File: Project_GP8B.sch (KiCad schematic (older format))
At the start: 16 parts, among them U1 74AHC05, U2 74AHC05, U3 74AHC1G02, U5 74AHC05

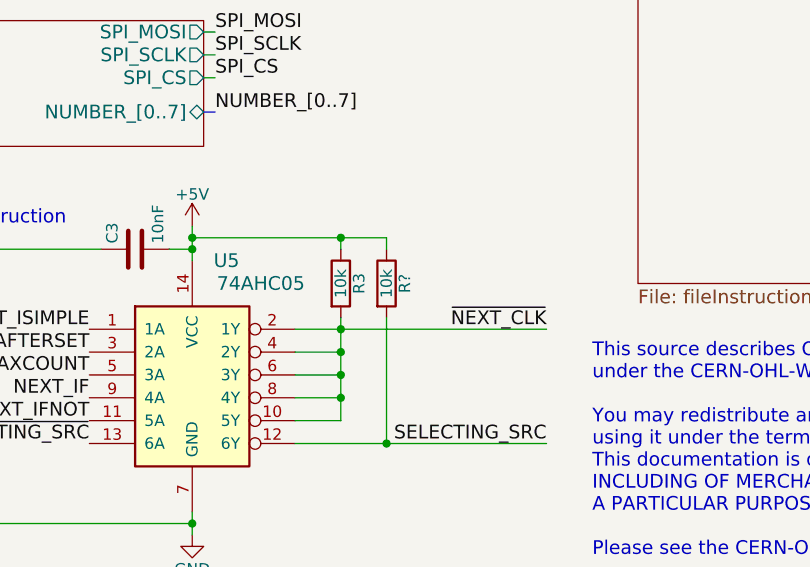
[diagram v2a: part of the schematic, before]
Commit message: Remove weird ghost bus in register
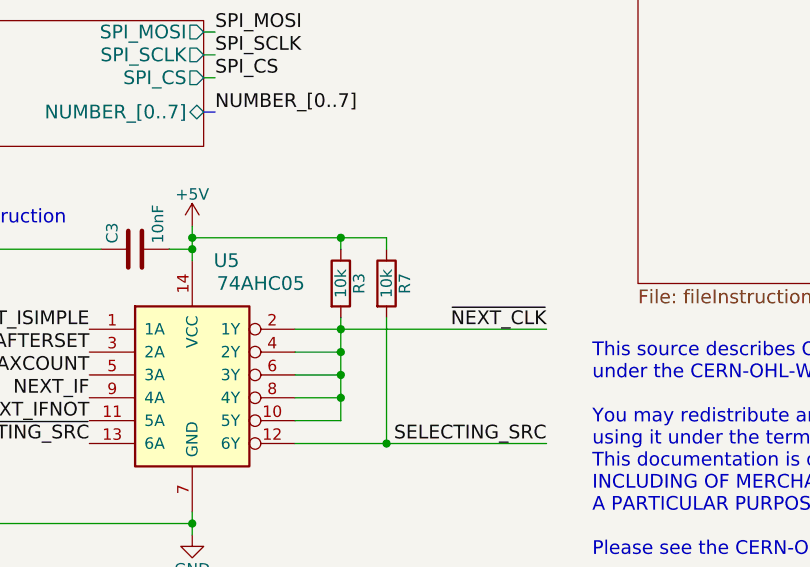
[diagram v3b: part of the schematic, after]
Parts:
- gave numbers to parts that had none: 1
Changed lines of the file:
@@
 SELECTING_SRC
 $Comp
-L Device:R R?
+L Device:R R7
 U 1 1 60507EBE
 P 6600 5250
-F 0 "R?" V 6680 5250 50  0000 C CNN
+F 0 "R7" V 6680 5250 50  0000 C CNN
 F 1 "10k" V 6600 5250 50  0000 C CNN
 F 2 "Resistor_SMD:R_0805_2012Metric" V 6530 5250 50  0001 C CNN

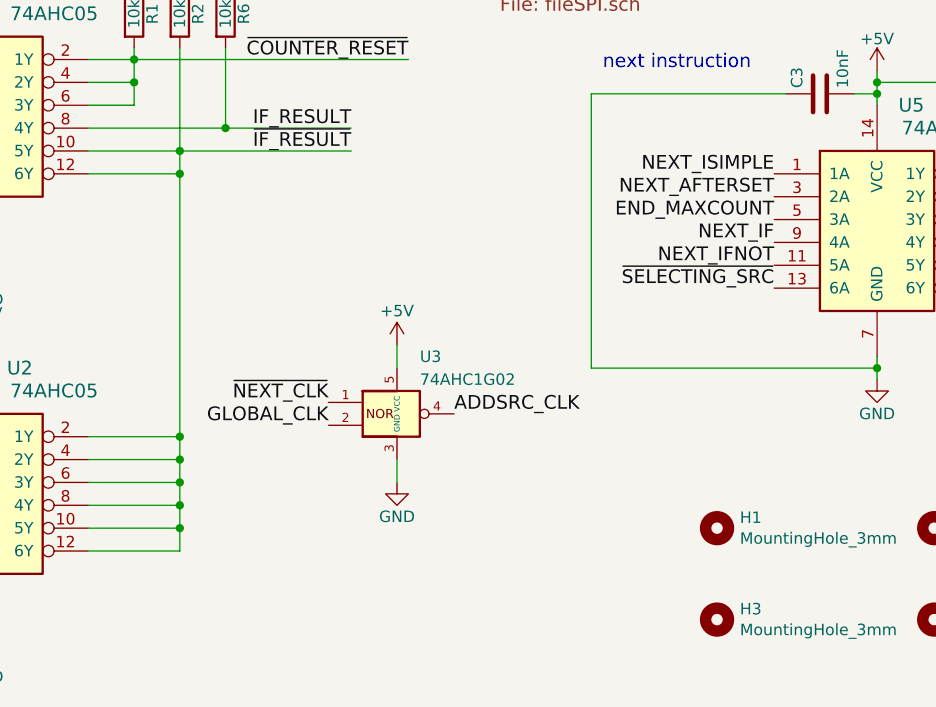
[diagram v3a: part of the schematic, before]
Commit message: Go next only if SRCVALUE, (complex instruction) #8 adding 74AHC1G08
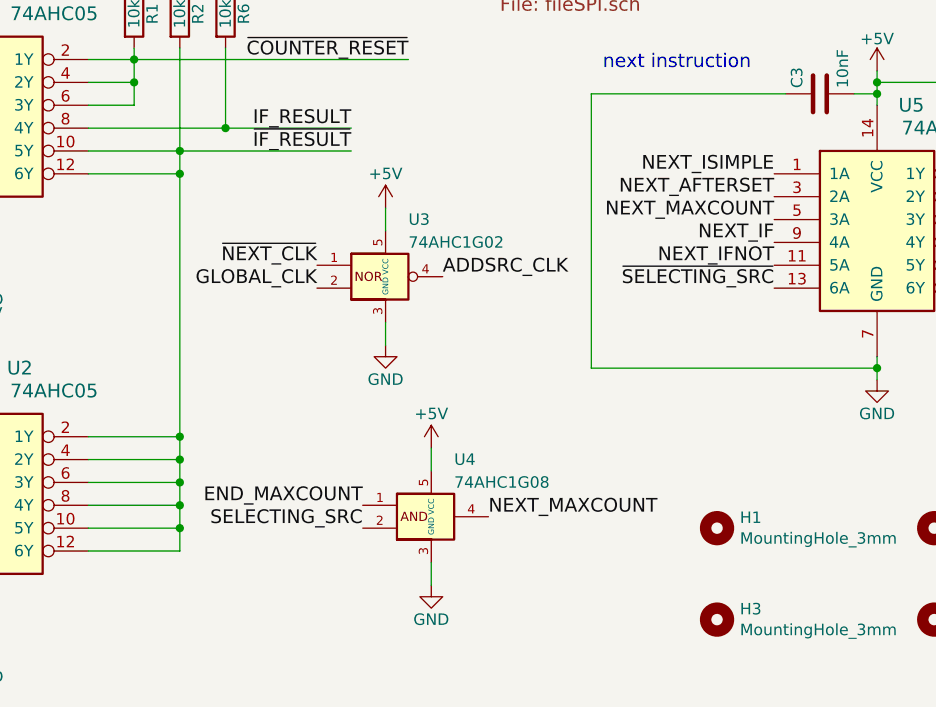
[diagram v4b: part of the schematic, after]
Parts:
- added U4: 74AHC1G08, symbol Custom:74AHC1G08
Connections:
- net +5V: now also U4.5 (VCC)
- net END_MAXCOUNT: now also U4.1; no longer U5.5 (3A)
- net GND: now also U4.3 (GND)
- net SELECTING_SRC: now also U4.2
- new net NEXT_MAXCOUNT: U4.4, U5.5 (3A)
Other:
- moved on the sheet: U3
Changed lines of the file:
@@
 L power:+5V #PWR07
 U 1 1 5B155C11
-P 3650 6200
-F 0 "#PWR07" H 3650 6050 50  0001 C CNN
-F 1 "+5V" H 3650 6350 50  0000 C CNN
-F 2 "" H 3650 6200 50  0001 C CNN
-F 3 "" H 3650 6200 50  0001 C CNN
-	1    3650 6200
+P 3600 5600
+F 0 "#PWR07" H 3600 5450 50  0001 C CNN
+F 1 "+5V" H 3600 5750 50  0000 C CNN
+F 2 "" H 3600 5600 50  0001 C CNN
+F 3 "" H 3600 5600 50  0001 C CNN
+	1    3600 5600
 	1    0    0    -1
 $EndComp
@@
 L power:GND #PWR010
 U 1 1 5B160445
-P 3650 6800
-F 0 "#PWR010" H 3650 6550 50  0001 C CNN
-F 1 "GND" H 3650 6650 50  0000 C CNN
-F 2 "" H 3650 6800 50  0001 C CNN
-F 3 "" H 3650 6800 50  0001 C CNN
-	1    3650 6800
+P 3600 6200
+F 0 "#PWR010" H 3600 5950 50  0001 C CNN
+F 1 "GND" H 3600 6050 50  0000 C CNN
+F 2 "" H 3600 6200 50  0001 C CNN
+F 3 "" H 3600 6200 50  0001 C CNN
+	1    3600 6200
 	1    0    0    -1
 $EndComp
@@
 $EndComp
 Wire Wire Line
-	3650 6700 3650 6800
+	3600 6100 3600 6200
 Wire Wire Line
 	4050 2550 4100 2550
@@
 Text Label 5300 5550 2    60   ~ 0
 NEXT_AFTERSET
-Text Label 5300 5650 2    60   ~ 0
-END_MAXCOUNT
 Text Label 5300 5750 2    60   ~ 0
 NEXT_IF
@@
 Wire Wire Line
 	2500 4950 3700 4950
-Text Label 3350 6550 2    60   ~ 0
+Text Label 3300 5950 2    60   ~ 0
 GLOBAL_CLK
-Text Label 3900 6500 0    60   ~ 0
+Text Label 3850 5900 0    60   ~ 0
 ADDSRC_CLK
-Text Label 3350 6450 2    60   ~ 0
+Text Label 3300 5850 2    60   ~ 0
 ~NEXT_CLK
 $Comp
 L Custom:74AHC1G02 U3
 U 1 1 605F1C2D
-P 3650 6500
-F 0 "U3" H 3750 6750 50  0000 L CNN
-F 1 "74AHC1G02" H 3750 6650 50  0000 L CNN
-F 2 "" H 3650 6500 50  0001 C CNN
-F 3 "https://assets.nexperia.com/documents/data-sheet/74AHC_AHCT1G02.pdf" H 3650 6500 50  0001 C CNN
-	1    3650 6500
-	1    0    0    -1
-$EndComp
-Wire Wire Line
-	3650 6200 3650 6300
+P 3600 5900
+F 0 "U3" H 3700 6150 50  0000 L CNN
+F 1 "74AHC1G02" H 3700 6050 50  0000 L CNN
+F 2 "" H 3600 5900 50  0001 C CNN
+F 3 "https://assets.nexperia.com/documents/data-sheet/74AHC_AHCT1G02.pdf" H 3600 5900 50  0001 C CNN
+	1    3600 5900
+	1    0    0    -1
+$EndComp
+Wire Wire Line
+	3600 5600 3600 5700
 Text Label 10300 1250 0    60   ~ 0
 ~SELECTING_SRC
@@
 Text Label 7650 2800 2    60   ~ 0
 SELECTING_SRC
+$Comp
+L Custom:74AHC1G08 U4
+U 1 1 6044588B
+P 3800 6950
+F 0 "U4" H 3900 7200 50  0000 L CNN
+F 1 "74AHC1G08" H 3900 7100 50  0000 L CNN
+F 2 "" H 3800 6950 50  0001 C CNN
+F 3 "https://assets.nexperia.com/documents/data-sheet/74AHC_AHCT1G08.pdf" H 3800 6950 50  0001 C CNN
+	1    3800 6950
+	1    0    0    -1
+$EndComp
+$Comp
+L power:+5V #PWR08
+U 1 1 604464C9
+P 3800 6650
+F 0 "#PWR08" H 3800 6500 50  0001 C CNN
+F 1 "+5V" H 3800 6800 50  0000 C CNN
+F 2 "" H 3800 6650 50  0001 C CNN
+F 3 "" H 3800 6650 50  0001 C CNN
+	1    3800 6650
+	1    0    0    -1
+$EndComp
+Wire Wire Line
+	3800 6650 3800 6750
+$Comp
+L power:GND #PWR09
+U 1 1 6044EE7C
+P 3800 7250
+F 0 "#PWR09" H 3800 7000 50  0001 C CNN
+F 1 "GND" H 3800 7100 50  0000 C CNN
+F 2 "" H 3800 7250 50  0001 C CNN
+F 3 "" H 3800 7250 50  0001 C CNN
+	1    3800 7250
+	1    0    0    -1
+$EndComp
+Wire Wire Line
+	3800 7150 3800 7250
+Text Label 3500 6900 2    60   ~ 0
+END_MAXCOUNT
+Text Label 3500 7000 2    60   ~ 0
+SELECTING_SRC
+Text Label 4050 6950 0    60   ~ 0
+NEXT_MAXCOUNT
+Text Label 5300 5650 2    60   ~ 0
+NEXT_MAXCOUNT
 Wire Bus Line
 	1700 2800 1700 3600

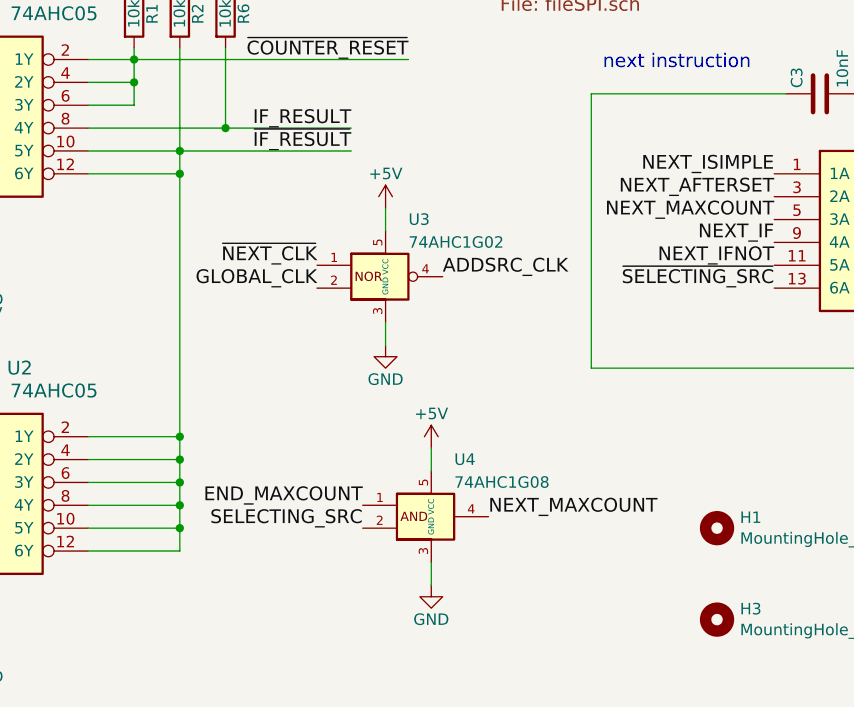
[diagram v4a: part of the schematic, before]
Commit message: Better decoupling #6
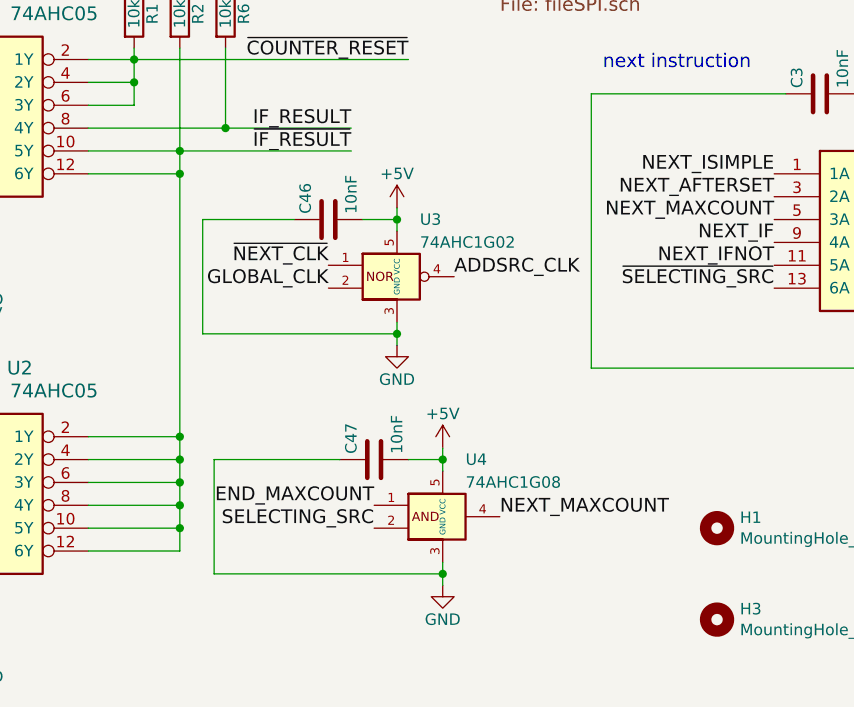
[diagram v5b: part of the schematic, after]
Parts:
- added C46, C47: 10nF, Capacitor_SMD:C_0805_2012Metric, symbol Device:C
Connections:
- net +5V: now also C46.2, C47.2
- net GND: now also C46.1, C47.1
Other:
- moved on the sheet: U3, U4
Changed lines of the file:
@@
 L power:+5V #PWR07
 U 1 1 5B155C11
-P 3600 5600
-F 0 "#PWR07" H 3600 5450 50  0001 C CNN
-F 1 "+5V" H 3600 5750 50  0000 C CNN
-F 2 "" H 3600 5600 50  0001 C CNN
-F 3 "" H 3600 5600 50  0001 C CNN
-	1    3600 5600
+P 3650 5600
+F 0 "#PWR07" H 3650 5450 50  0001 C CNN
+F 1 "+5V" H 3650 5750 50  0000 C CNN
+F 2 "" H 3650 5600 50  0001 C CNN
+F 3 "" H 3650 5600 50  0001 C CNN
+	1    3650 5600
 	1    0    0    -1
 $EndComp
@@
 L power:GND #PWR010
 U 1 1 5B160445
-P 3600 6200
-F 0 "#PWR010" H 3600 5950 50  0001 C CNN
-F 1 "GND" H 3600 6050 50  0000 C CNN
-F 2 "" H 3600 6200 50  0001 C CNN
-F 3 "" H 3600 6200 50  0001 C CNN
-	1    3600 6200
+P 3650 6200
+F 0 "#PWR010" H 3650 5950 50  0001 C CNN
+F 1 "GND" H 3650 6050 50  0000 C CNN
+F 2 "" H 3650 6200 50  0001 C CNN
+F 3 "" H 3650 6200 50  0001 C CNN
+	1    3650 6200
 	1    0    0    -1
 $EndComp
@@
 $EndComp
 Wire Wire Line
-	3600 6100 3600 6200
+	3650 6100 3650 6150
 Wire Wire Line
 	4050 2550 4100 2550
@@
 Wire Wire Line
 	2500 4950 3700 4950
-Text Label 3300 5950 2    60   ~ 0
+Text Label 3350 5950 2    60   ~ 0
 GLOBAL_CLK
-Text Label 3850 5900 0    60   ~ 0
+Text Label 3900 5900 0    60   ~ 0
 ADDSRC_CLK
-Text Label 3300 5850 2    60   ~ 0
+Text Label 3350 5850 2    60   ~ 0
 ~NEXT_CLK
 $Comp
 L Custom:74AHC1G02 U3
 U 1 1 605F1C2D
-P 3600 5900
-F 0 "U3" H 3700 6150 50  0000 L CNN
-F 1 "74AHC1G02" H 3700 6050 50  0000 L CNN
-F 2 "" H 3600 5900 50  0001 C CNN
-F 3 "https://assets.nexperia.com/documents/data-sheet/74AHC_AHCT1G02.pdf" H 3600 5900 50  0001 C CNN
-	1    3600 5900
-	1    0    0    -1
-$EndComp
-Wire Wire Line
-	3600 5600 3600 5700
+P 3650 5900
+F 0 "U3" H 3750 6150 50  0000 L CNN
+F 1 "74AHC1G02" H 3750 6050 50  0000 L CNN
+F 2 "" H 3650 5900 50  0001 C CNN
+F 3 "https://assets.nexperia.com/documents/data-sheet/74AHC_AHCT1G02.pdf" H 3650 5900 50  0001 C CNN
+	1    3650 5900
+	1    0    0    -1
+$EndComp
+Wire Wire Line
+	3650 5600 3650 5650
 Text Label 10300 1250 0    60   ~ 0
 ~SELECTING_SRC
@@
 L Custom:74AHC1G08 U4
 U 1 1 6044588B
-P 3800 6950
-F 0 "U4" H 3900 7200 50  0000 L CNN
-F 1 "74AHC1G08" H 3900 7100 50  0000 L CNN
-F 2 "" H 3800 6950 50  0001 C CNN
-F 3 "https://assets.nexperia.com/documents/data-sheet/74AHC_AHCT1G08.pdf" H 3800 6950 50  0001 C CNN
-	1    3800 6950
+P 3850 6950
+F 0 "U4" H 3950 7200 50  0000 L CNN
+F 1 "74AHC1G08" H 3950 7100 50  0000 L CNN
+F 2 "" H 3850 6950 50  0001 C CNN
+F 3 "https://assets.nexperia.com/documents/data-sheet/74AHC_AHCT1G08.pdf" H 3850 6950 50  0001 C CNN
+	1    3850 6950
 	1    0    0    -1
 $EndComp
@@
 L power:+5V #PWR08
 U 1 1 604464C9
-P 3800 6650
-F 0 "#PWR08" H 3800 6500 50  0001 C CNN
-F 1 "+5V" H 3800 6800 50  0000 C CNN
-F 2 "" H 3800 6650 50  0001 C CNN
-F 3 "" H 3800 6650 50  0001 C CNN
-	1    3800 6650
-	1    0    0    -1
-$EndComp
-Wire Wire Line
-	3800 6650 3800 6750
+P 3850 6650
+F 0 "#PWR08" H 3850 6500 50  0001 C CNN
+F 1 "+5V" H 3850 6800 50  0000 C CNN
+F 2 "" H 3850 6650 50  0001 C CNN
+F 3 "" H 3850 6650 50  0001 C CNN
+	1    3850 6650
+	1    0    0    -1
+$EndComp
+Wire Wire Line
+	3850 6650 3850 6700
 $Comp
 L power:GND #PWR09
 U 1 1 6044EE7C
-P 3800 7250
-F 0 "#PWR09" H 3800 7000 50  0001 C CNN
-F 1 "GND" H 3800 7100 50  0000 C CNN
-F 2 "" H 3800 7250 50  0001 C CNN
-F 3 "" H 3800 7250 50  0001 C CNN
-	1    3800 7250
-	1    0    0    -1
-$EndComp
-Wire Wire Line
-	3800 7150 3800 7250
-Text Label 3500 6900 2    60   ~ 0
+P 3850 7250
+F 0 "#PWR09" H 3850 7000 50  0001 C CNN
+F 1 "GND" H 3850 7100 50  0000 C CNN
+F 2 "" H 3850 7250 50  0001 C CNN
+F 3 "" H 3850 7250 50  0001 C CNN
+	1    3850 7250
+	1    0    0    -1
+$EndComp
+Wire Wire Line
+	3850 7150 3850 7200
+Text Label 3550 6900 2    60   ~ 0
 END_MAXCOUNT
-Text Label 3500 7000 2    60   ~ 0
+Text Label 3550 7000 2    60   ~ 0
 SELECTING_SRC
-Text Label 4050 6950 0    60   ~ 0
+Text Label 4100 6950 0    60   ~ 0
 NEXT_MAXCOUNT
 Text Label 5300 5650 2    60   ~ 0
 NEXT_MAXCOUNT
+$Comp
+L Device:C C46
+U 1 1 60540AE9
+P 3350 5650
+F 0 "C46" H 3375 5750 50  0000 L CNN
+F 1 "10nF" H 3375 5550 50  0000 L CNN
+F 2 "Capacitor_SMD:C_0805_2012Metric" H 3388 5500 50  0001 C CNN
+F 3 "" H 3350 5650 50  0001 C CNN
+	1    3350 5650
+	0    -1   -1   0
+$EndComp
+$Comp
+L Device:C C47
+U 1 1 60540DD5
+P 3550 6700
+F 0 "C47" H 3575 6800 50  0000 L CNN
+F 1 "10nF" H 3575 6600 50  0000 L CNN
+F 2 "Capacitor_SMD:C_0805_2012Metric" H 3588 6550 50  0001 C CNN
+F 3 "" H 3550 6700 50  0001 C CNN
+	1    3550 6700
+	0    -1   -1   0
+$EndComp
+Wire Wire Line
+	3200 5650 2800 5650
+Wire Wire Line
+	2800 5650 2800 6150
+Wire Wire Line
+	2800 6150 3650 6150
+Connection ~ 3650 6150
+Wire Wire Line
+	3650 6150 3650 6200
+Wire Wire Line
+	3500 5650 3650 5650
+Connection ~ 3650 5650
+Wire Wire Line
+	3650 5650 3650 5700
+Wire Wire Line
+	3850 6700 3700 6700
+Connection ~ 3850 6700
+Wire Wire Line
+	3850 6700 3850 6750
+Wire Wire Line
+	3400 6700 2850 6700
+Wire Wire Line
+	2850 6700 2850 7200
+Wire Wire Line
+	2850 7200 3850 7200
+Connection ~ 3850 7200
+Wire Wire Line
+	3850 7200 3850 7250
 Wire Bus Line
 	1700 2800 1700 3600

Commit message: Component association (#7)
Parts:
- U3, U4: footprint (none) -> Package_TO_SOT_SMD:SOT-23-5
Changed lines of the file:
@@
 F 0 "U3" H 3750 6150 50  0000 L CNN
 F 1 "74AHC1G02" H 3750 6050 50  0000 L CNN
-F 2 "" H 3650 5900 50  0001 C CNN
+F 2 "Package_TO_SOT_SMD:SOT-23-5" H 3650 5900 50  0001 C CNN
 F 3 "https://assets.nexperia.com/documents/data-sheet/74AHC_AHCT1G02.pdf" H 3650 5900 50  0001 C CNN
 	1    3650 5900
@@
 F 0 "U4" H 3950 7200 50  0000 L CNN
 F 1 "74AHC1G08" H 3950 7100 50  0000 L CNN
-F 2 "" H 3850 6950 50  0001 C CNN
+F 2 "Package_TO_SOT_SMD:SOT-23-5" H 3850 6950 50  0001 C CNN
 F 3 "https://assets.nexperia.com/documents/data-sheet/74AHC_AHCT1G08.pdf" H 3850 6950 50  0001 C CNN
 	1    3850 6950
